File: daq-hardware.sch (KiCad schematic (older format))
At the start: 25 parts, among them J1 USB_B, J2 Micro_SD_Card_Det_Hirose_DM3AT, Q1 MMDT2222A, SW1 SW1, SW2 SW1, U1 CP2102N-A01-GQFN24, U2 ESP32-WROOM-32D

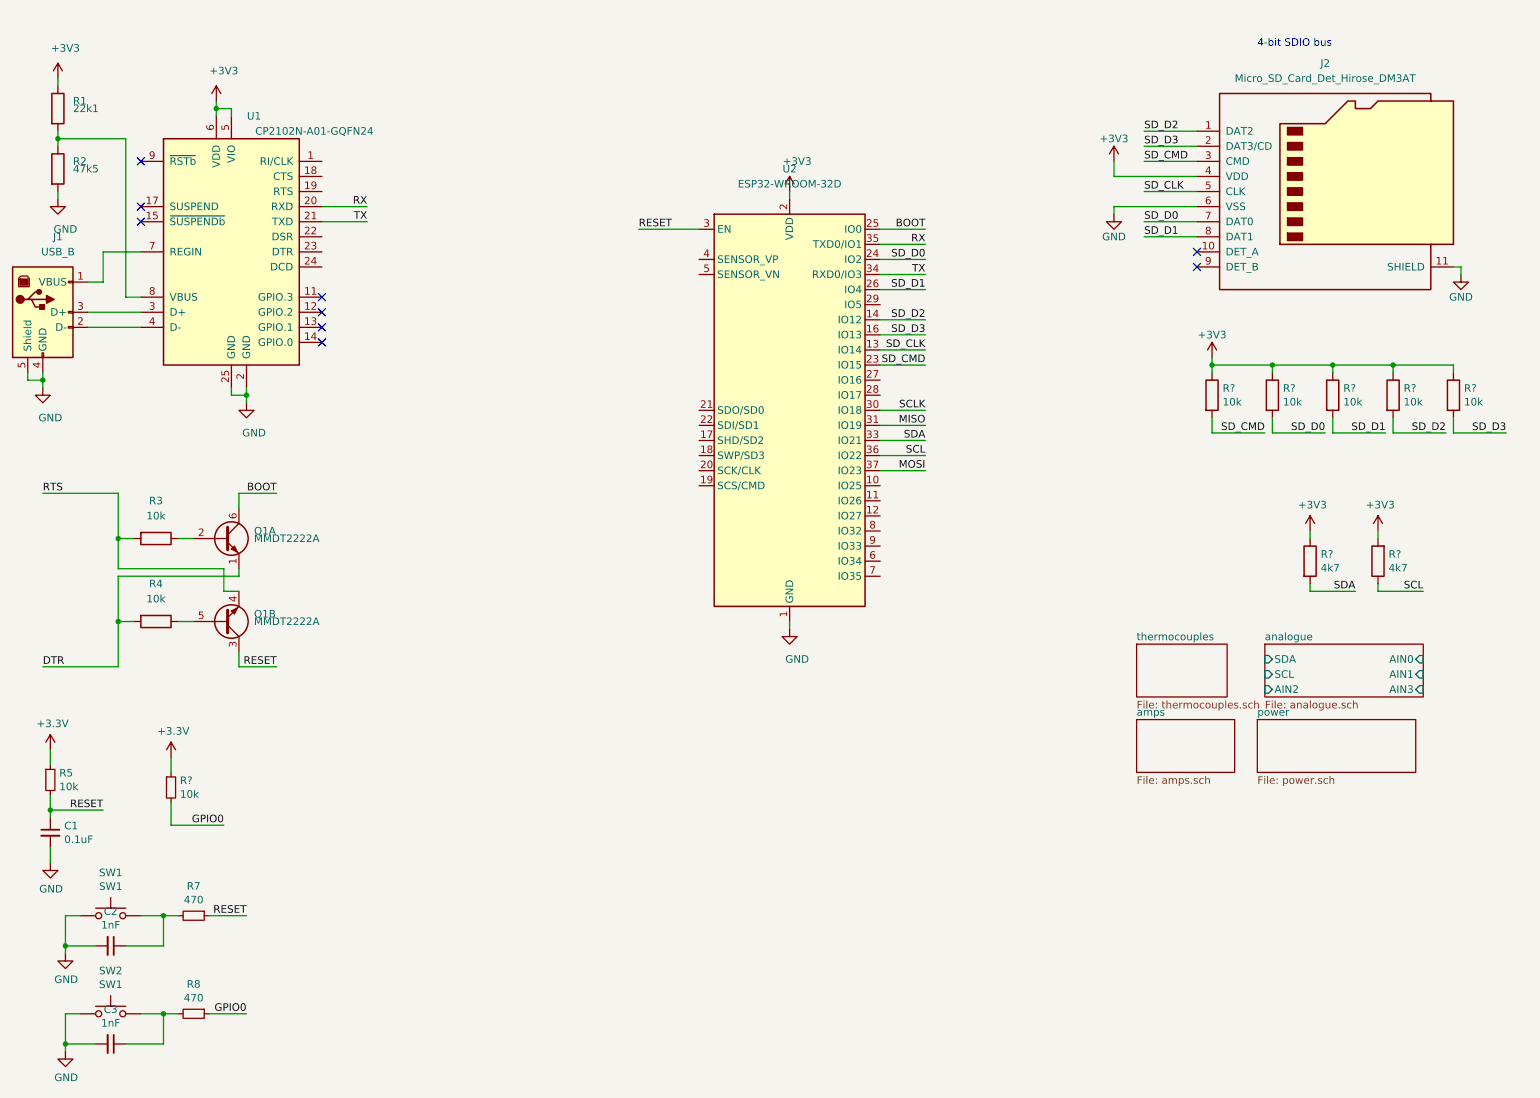
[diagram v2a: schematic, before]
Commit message: Preliminary pin mapping and amended thermocouple hierarchical sheets
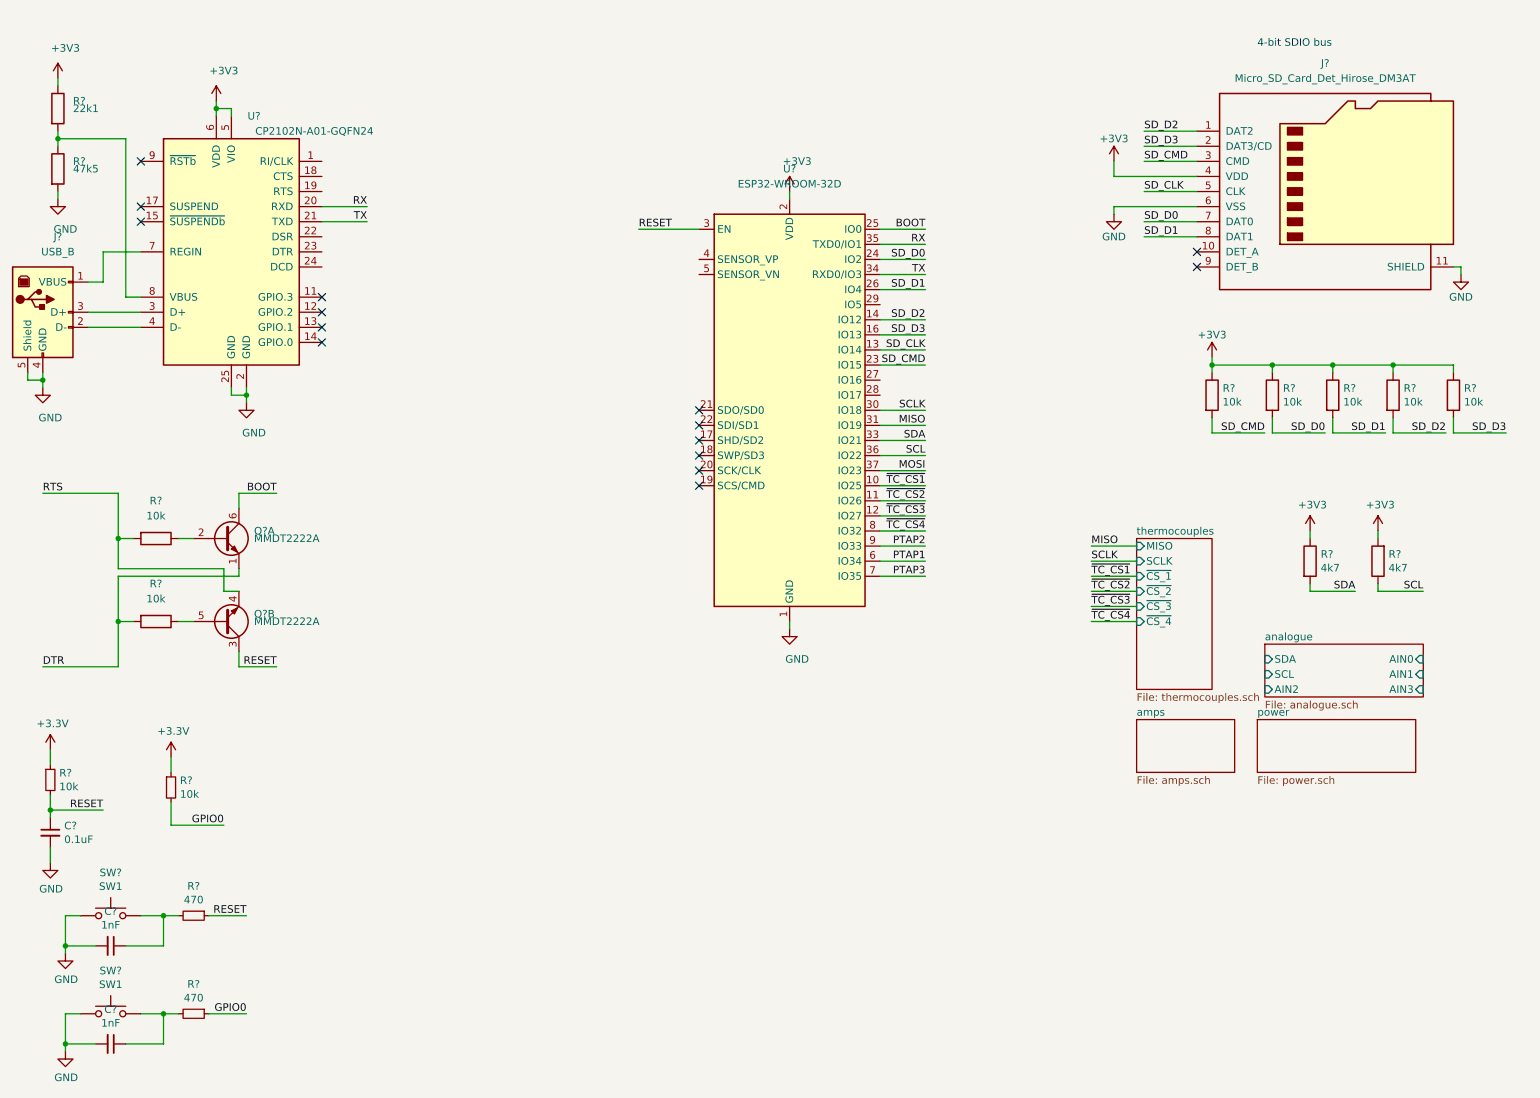
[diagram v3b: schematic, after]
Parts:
- renumbered C1 to C?, C2 to C?, C3 to C?, J1 to J?, J2 to J?, Q1 to Q?, R1 to R?, R2 to R?, R3 to R?, R4 to R?, R5 to R?, R7 to R?, R8 to R?, SW1 to SW?, SW2 to SW?, U2 to U?, U1 to U?
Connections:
- net ~TC_CS1: now reaches U?.10 (IO25)
- net ~TC_CS2: now reaches U?.11 (IO26)
- net ~TC_CS3: now reaches U?.12 (IO27)
- net PTAP1: now reaches U?.6 (IO34)
- net PTAP3: now reaches U?.7 (IO35)
- net ~TC_CS4: now reaches U?.8 (IO32)
- net PTAP2: now reaches U?.9 (IO33)
- no-connect marks 9 -> 15
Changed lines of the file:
@@
 $EndDescr
 $Comp
-L power:+3V3 #PWR0101
+L power:+3V3 #PWR?
 U 1 1 5DA618F4
 P 6300 1750
-F 0 "#PWR0101" H 6300 1600 50  0001 C CNN
+F 0 "#PWR?" H 6300 1600 50  0001 C CNN
 F 1 "+3V3" H 6350 1950 50  0000 C CNN
 F 2 "" H 6300 1750 50  0001 C CNN
@@
 	6300 1750 6300 1800
 $Comp
-L power:GND #PWR0102
+L power:GND #PWR?
 U 1 1 5DA62185
 P 6300 4650
-F 0 "#PWR0102" H 6300 4400 50  0001 C CNN
+F 0 "#PWR?" H 6300 4400 50  0001 C CNN
 F 1 "GND" H 6350 4450 50  0000 C CNN
 F 2 "" H 6300 4650 50  0001 C CNN
@@
 	6300 4650 6300 4600
 $Comp
-L Connector:USB_B J1
+L Connector:USB_B J?
 U 1 1 5DA63605
 P 1350 2550
-F 0 "J1" H 1450 3050 50  0000 C CNN
+F 0 "J?" H 1450 3050 50  0000 C CNN
 F 1 "USB_B" H 1450 2950 50  0000 C CNN
 F 2 "Connector_USB:USB_B_OST_USB-B1HSxx_Horizontal" H 1500 2500 50  0001 C CNN
@@
 $EndComp
 $Comp
-L Interface_USB:CP2102N-A01-GQFN24 U1
+L Interface_USB:CP2102N-A01-GQFN24 U?
 U 1 1 5DA64A7C
 P 2600 2150
-F 0 "U1" H 2750 3050 50  0000 C CNN
+F 0 "U?" H 2750 3050 50  0000 C CNN
 F 1 "CP2102N-A01-GQFN24" H 3150 2950 50  0000 C CNN
 F 2 "Package_DFN_QFN:QFN-24-1EP_4x4mm_P0.5mm_EP2.6x2.6mm" H 3050 1350 50  0001 L CNN
@@
 	1650 2650 2000 2650
 $Comp
-L power:GND #PWR0103
+L power:GND #PWR?
 U 1 1 5DA6844F
 P 2700 3150
-F 0 "#PWR0103" H 2700 2900 50  0001 C CNN
+F 0 "#PWR?" H 2700 2900 50  0001 C CNN
 F 1 "GND" H 2750 2950 50  0000 C CNN
 F 2 "" H 2700 3150 50  0001 C CNN
@@
 	2700 3100 2700 3050
 $Comp
-L power:GND #PWR0104
+L power:GND #PWR?
 U 1 1 5DA68DCE
 P 1350 3050
-F 0 "#PWR0104" H 1350 2800 50  0001 C CNN
+F 0 "#PWR?" H 1350 2800 50  0001 C CNN
 F 1 "GND" H 1400 2850 50  0000 C CNN
 F 2 "" H 1350 3050 50  0001 C CNN
@@
 Connection ~ 1350 3000
 $Comp
-L power:+3V3 #PWR0105
+L power:+3V3 #PWR?
 U 1 1 5DA69782
 P 2500 1150
-F 0 "#PWR0105" H 2500 1000 50  0001 C CNN
+F 0 "#PWR?" H 2500 1000 50  0001 C CNN
 F 1 "+3V3" H 2550 1350 50  0000 C CNN
 F 2 "" H 2500 1150 50  0001 C CNN
@@
 	2500 1200 2500 1250
 $Comp
-L RF_Module:ESP32-WROOM-32D U2
+L RF_Module:ESP32-WROOM-32D U?
 U 1 1 5DA60666
 P 6300 3200
-F 0 "U2" H 6300 4800 50  0000 C CNN
+F 0 "U?" H 6300 4800 50  0000 C CNN
 F 1 "ESP32-WROOM-32D" H 6300 4700 50  0000 C CNN
 F 2 "RF_Module:ESP32-WROOM-32" H 6300 1700 50  0001 C CNN
@@
 	1750 2150 2000 2150
 $Comp
-L Device:R R1
+L Device:R R?
 U 1 1 5DA6B300
 P 1450 1200
-F 0 "R1" H 1550 1250 50  0000 L CNN
+F 0 "R?" H 1550 1250 50  0000 L CNN
 F 1 "22k1" H 1550 1200 50  0000 L CNN
 F 2 "" V 1380 1200 50  0001 C CNN
@@
 $EndComp
 $Comp
-L Device:R R2
+L Device:R R?
 U 1 1 5DA6BB78
 P 1450 1600
-F 0 "R2" H 1550 1650 50  0000 L CNN
+F 0 "R?" H 1550 1650 50  0000 L CNN
 F 1 "47k5" H 1550 1600 50  0000 L CNN
 F 2 "" V 1380 1600 50  0001 C CNN
@@
 	1450 1400 1450 1450
 $Comp
-L power:GND #PWR0106
+L power:GND #PWR?
 U 1 1 5DA6CE1F
 P 1450 1800
-F 0 "#PWR0106" H 1450 1550 50  0001 C CNN
+F 0 "#PWR?" H 1450 1550 50  0001 C CNN
 F 1 "GND" H 1500 1600 50  0000 C CNN
 F 2 "" H 1450 1800 50  0001 C CNN
@@
 	1450 1800 1450 1750
 $Comp
-L power:+3V3 #PWR0107
+L power:+3V3 #PWR?
 U 1 1 5DA6D946
 P 1450 1000
-F 0 "#PWR0107" H 1450 850 50  0001 C CNN
+F 0 "#PWR?" H 1450 850 50  0001 C CNN
 F 1 "+3V3" H 1500 1200 50  0000 C CNN
 F 2 "" H 1450 1000 50  0001 C CNN
@@
 TX
 $Comp
-L Connector:Micro_SD_Card_Det_Hirose_DM3AT J2
+L Connector:Micro_SD_Card_Det_Hirose_DM3AT J?
 U 1 1 5DA72DEE
 P 9900 1750
-F 0 "J2" H 9850 2600 50  0000 C CNN
+F 0 "J?" H 9850 2600 50  0000 C CNN
 F 1 "Micro_SD_Card_Det_Hirose_DM3AT" H 9850 2500 50  0000 C CNN
 F 2 "Connector_Card:microSD_HC_Hirose_DM3AT-SF-PEJM5" H 11950 2450 50  0001 C CNN
@@
 $EndComp
 $Comp
-L power:+3V3 #PWR0108
+L power:+3V3 #PWR?
 U 1 1 5DA74F5A
 P 8450 1550
-F 0 "#PWR0108" H 8450 1400 50  0001 C CNN
+F 0 "#PWR?" H 8450 1400 50  0001 C CNN
 F 1 "+3V3" H 8450 1700 50  0000 C CNN
 F 2 "" H 8450 1550 50  0001 C CNN
@@
 	8450 1650 9000 1650
 $Comp
-L power:GND #PWR0109
+L power:GND #PWR?
 U 1 1 5DA76764
 P 8450 1900
-F 0 "#PWR0109" H 8450 1650 50  0001 C CNN
+F 0 "#PWR?" H 8450 1650 50  0001 C CNN
 F 1 "GND" H 8450 1750 50  0000 C CNN
 F 2 "" H 8450 1900 50  0001 C CNN
@@
 	8450 1850 9000 1850
 $Comp
-L Transistor_BJT:MMDT2222A Q1
+L Transistor_BJT:MMDT2222A Q?
 U 1 1 5DA77BBC
 P 2550 4050
-F 0 "Q1" H 2750 4100 50  0000 L CNN
+F 0 "Q?" H 2750 4100 50  0000 L CNN
 F 1 "MMDT2222A" H 2750 4050 50  0000 L CNN
 F 2 "Package_TO_SOT_SMD:SOT-363_SC-70-6" H 2750 4150 50  0001 C CNN
@@
 $EndComp
 $Comp
-L Transistor_BJT:MMDT2222A Q1
+L Transistor_BJT:MMDT2222A Q?
 U 2 1 5DA7899D
 P 2550 4600
-F 0 "Q1" H 2750 4550 50  0000 L CNN
+F 0 "Q?" H 2750 4550 50  0000 L CNN
 F 1 "MMDT2222A" H 2750 4600 50  0000 L CNN
 F 2 "Package_TO_SOT_SMD:SOT-363_SC-70-6" H 2750 4700 50  0001 C CNN
@@
 $EndComp
 $Comp
-L Device:R R3
+L Device:R R?
 U 1 1 5DA7B0F5
 P 2100 4050
-F 0 "R3" V 1850 4050 50  0000 C CNN
+F 0 "R?" V 1850 4050 50  0000 C CNN
 F 1 "10k" V 1950 4050 50  0000 C CNN
 F 2 "Resistor_SMD:R_0603_1608Metric" V 2030 4050 50  0001 C CNN
@@
 $EndComp
 $Comp
-L Device:R R4
+L Device:R R?
 U 1 1 5DA7B96F
 P 2100 4600
-F 0 "R4" V 1850 4600 50  0000 C CNN
+F 0 "R?" V 1850 4600 50  0000 C CNN
 F 1 "10k" V 1950 4600 50  0000 C CNN
 F 2 "Resistor_SMD:R_0603_1608Metric" V 2030 4600 50  0001 C CNN
@@
 MOSI
 $Comp
-L Device:R_Small R5
+L Device:R_Small R?
 U 1 1 5DBE20E6
 P 1400 5650
-F 0 "R5" H 1459 5696 50  0000 L CNN
+F 0 "R?" H 1459 5696 50  0000 L CNN
 F 1 "10k" H 1459 5605 50  0000 L CNN
 F 2 "" H 1400 5650 50  0001 C CNN
@@
 $EndComp
 $Comp
-L Device:C_Small C1
+L Device:C_Small C?
 U 1 1 5DBE24AB
 P 1400 6000
-F 0 "C1" H 1492 6046 50  0000 L CNN
+F 0 "C?" H 1492 6046 50  0000 L CNN
 F 1 "0.1uF" H 1492 5955 50  0000 L CNN
 F 2 "" H 1400 6000 50  0001 C CNN
@@
 	1400 5850 1400 5900
 $Comp
-L power:+3.3V #PWR0112
+L power:+3.3V #PWR?
 U 1 1 5DBE5B8C
 P 1400 5450
-F 0 "#PWR0112" H 1400 5300 50  0001 C CNN
+F 0 "#PWR?" H 1400 5300 50  0001 C CNN
 F 1 "+3.3V" H 1415 5623 50  0000 C CNN
 F 2 "" H 1400 5450 50  0001 C CNN
@@
 	1400 5450 1400 5550
 $Comp
-L power:GND #PWR0113
+L power:GND #PWR?
 U 1 1 5DBE7B6D
 P 1400 6200
-F 0 "#PWR0113" H 1400 5950 50  0001 C CNN
+F 0 "#PWR?" H 1400 5950 50  0001 C CNN
 F 1 "GND" H 1405 6027 50  0000 C CNN
 F 2 "" H 1400 6200 50  0001 C CNN
@@
 RESET
 $Comp
-L power:+3.3V #PWR0114
+L power:+3.3V #PWR?
 U 1 1 5DBEA935
 P 2200 5500
-F 0 "#PWR0114" H 2200 5350 50  0001 C CNN
+F 0 "#PWR?" H 2200 5350 50  0001 C CNN
 F 1 "+3.3V" H 2215 5673 50  0000 C CNN
 F 2 "" H 2200 5500 50  0001 C CNN
@@
 GPIO0
 $Comp
-L Switch:SW_Push SW1
+L Switch:SW_Push SW?
 U 1 1 5DBEEFD5
 P 1800 6550
-F 0 "SW1" H 1800 6835 50  0000 C CNN
+F 0 "SW?" H 1800 6835 50  0000 C CNN
 F 1 "SW1" H 1800 6744 50  0000 C CNN
 F 2 "" H 1800 6750 50  0001 C CNN
@@
 $EndComp
 $Comp
-L power:GND #PWR0115
+L power:GND #PWR?
 U 1 1 5DBF1A42
 P 1500 6800
-F 0 "#PWR0115" H 1500 6550 50  0001 C CNN
+F 0 "#PWR?" H 1500 6550 50  0001 C CNN
 F 1 "GND" H 1505 6627 50  0000 C CNN
 F 2 "" H 1500 6800 50  0001 C CNN
@@
 $EndComp
 $Comp
-L Device:C_Small C2
+L Device:C_Small C?
 U 1 1 5DBF1E6A
 P 1800 6750
-F 0 "C2" V 1571 6750 50  0000 C CNN
+F 0 "C?" V 1571 6750 50  0000 C CNN
 F 1 "1nF" V 1662 6750 50  0000 C CNN
 F 2 "" H 1800 6750 50  0001 C CNN
@@
 $EndComp
 $Comp
-L Device:R_Small R7
+L Device:R_Small R?
 U 1 1 5DBF243C
 P 2350 6550
-F 0 "R7" V 2154 6550 50  0000 C CNN
+F 0 "R?" V 2154 6550 50  0000 C CNN
 F 1 "470" V 2245 6550 50  0000 C CNN
 F 2 "" H 2350 6550 50  0001 C CNN
@@
 	2700 6550 2450 6550
 $Comp
-L Switch:SW_Push SW2
+L Switch:SW_Push SW?
 U 1 1 5DBFE9BD
 P 1800 7200
-F 0 "SW2" H 1800 7485 50  0000 C CNN
+F 0 "SW?" H 1800 7485 50  0000 C CNN
 F 1 "SW1" H 1800 7394 50  0000 C CNN
 F 2 "" H 1800 7400 50  0001 C CNN
@@
 $EndComp
 $Comp
-L power:GND #PWR0116
+L power:GND #PWR?
 U 1 1 5DBFE9C3
 P 1500 7450
-F 0 "#PWR0116" H 1500 7200 50  0001 C CNN
+F 0 "#PWR?" H 1500 7200 50  0001 C CNN
 F 1 "GND" H 1505 7277 50  0000 C CNN
 F 2 "" H 1500 7450 50  0001 C CNN
@@
 $EndComp
 $Comp
-L Device:C_Small C3
+L Device:C_Small C?
 U 1 1 5DBFE9C9
 P 1800 7400
-F 0 "C3" V 1571 7400 50  0000 C CNN
+F 0 "C?" V 1571 7400 50  0000 C CNN
 F 1 "1nF" V 1662 7400 50  0000 C CNN
 F 2 "" H 1800 7400 50  0001 C CNN
@@
 $EndComp
 $Comp
-L Device:R_Small R8
+L Device:R_Small R?
 U 1 1 5DBFE9CF
 P 2350 7200
-F 0 "R8" V 2154 7200 50  0000 C CNN
+F 0 "R?" V 2154 7200 50  0000 C CNN
 F 1 "470" V 2245 7200 50  0000 C CNN
 F 2 "" H 2350 7200 50  0001 C CNN
@@
 $EndSheet
 $Sheet
-S 8600 4750 600  350
+S 8600 4050 500  1000
 U 5DAD2AA3
 F0 "thermocouples" 50
 F1 "thermocouples.sch" 50
+F2 "~CS_1" I L 8600 4300 50
+F3 "~CS_2" I L 8600 4400 50
+F4 "~CS_3" I L 8600 4500 50
+F5 "SCLK" I L 8600 4200 50
+F6 "MISO" I L 8600 4100 50
+F7 "~CS_4" I L 8600 4600 50
 $EndSheet
 Wire Wire Line
@@
 Text Notes 9400 800  0    50   ~ 0
 4-bit SDIO bus
+Wire Wire Line
+	6900 3700 7200 3700
+Wire Wire Line
+	6900 3800 7200 3800
+Text Label 7200 3700 2    50   ~ 0
+~TC_CS1
+Text Label 7200 3800 2    50   ~ 0
+~TC_CS2
+Text Label 8300 4100 0    50   ~ 0
+MISO
+Wire Wire Line
+	8300 4100 8600 4100
+Text Label 8300 4200 0    50   ~ 0
+SCLK
+Wire Wire Line
+	8300 4200 8600 4200
+Text Label 8300 4300 0    50   ~ 0
+~TC_CS1
+Wire Wire Line
+	8300 4300 8600 4300
+Text Label 8300 4400 0    50   ~ 0
+~TC_CS2
+Wire Wire Line
+	8300 4400 8600 4400
+Wire Wire Line
+	6900 4200 7200 4200
+Wire Wire Line
+	6900 4100 7200 4100
+Text Label 7200 4200 2    50   ~ 0
+PTAP1
+Text Label 7200 4100 2    50   ~ 0
+PTAP2
+Wire Wire Line
+	6900 4300 7200 4300
+Text Label 7200 4300 2    50   ~ 0
+PTAP3
+Wire Wire Line
+	6900 3900 7200 3900
+Text Label 7200 3900 2    50   ~ 0
+~TC_CS3
+Wire Wire Line
+	6900 4000 7200 4000
+Text Label 7200 4000 2    50   ~ 0
+~TC_CS4
+Wire Wire Line
+	8600 4500 8300 4500
+Text Label 8300 4500 0    50   ~ 0
+~TC_CS3
+Wire Wire Line
+	8600 4600 8300 4600
+Text Label 8300 4600 0    50   ~ 0
+~TC_CS4
+NoConn ~ 5700 3200
+NoConn ~ 5700 3300
+NoConn ~ 5700 3400
+NoConn ~ 5700 3500
+NoConn ~ 5700 3600
+NoConn ~ 5700 3700
 $EndSCHEMATC

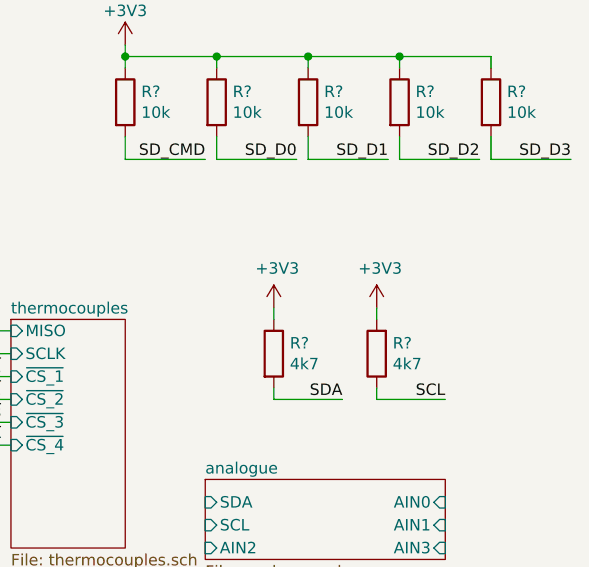
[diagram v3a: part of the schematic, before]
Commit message: Added and locked mounting holes
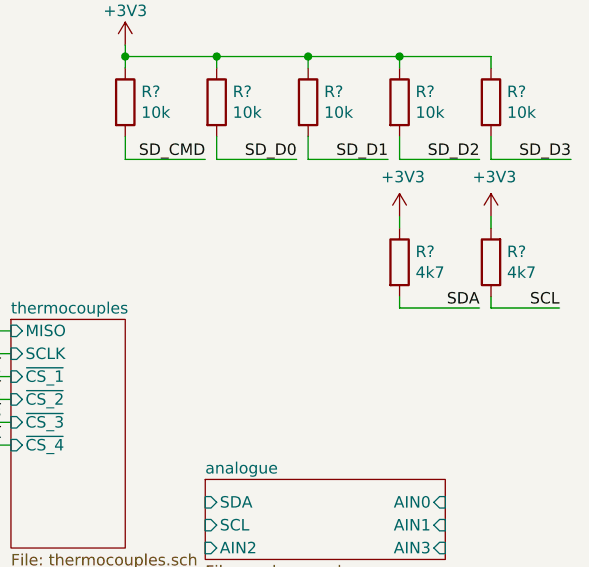
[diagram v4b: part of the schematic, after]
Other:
- moved on the sheet: R?
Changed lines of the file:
@@
 SCL
 Wire Wire Line
-	9750 4400 10050 4400
+	10300 4000 10650 4000
 Wire Wire Line
-	10200 4400 10500 4400
-Text Label 10050 4400 2    50   ~ 0
+	10700 4000 11000 4000
+Text Label 10650 4000 2    50   ~ 0
 SDA
-Text Label 10500 4400 2    50   ~ 0
+Text Label 11000 4000 2    50   ~ 0
 SCL
 $Comp
 L Device:R R?
 U 1 1 5DB5090D
-P 9750 4200
+P 10300 3800
 AR Path="/5DA926B9/5DB5090D" Ref="R?"  Part="1"
 AR Path="/5DB5090D" Ref="R?"  Part="1"
-F 0 "R?" H 9820 4246 50  0000 L CNN
-F 1 "4k7" H 9820 4155 50  0000 L CNN
-F 2 "" V 9680 4200 50  0001 C CNN
-F 3 "~" H 9750 4200 50  0001 C CNN
-	1    9750 4200
+F 0 "R?" H 10370 3846 50  0000 L CNN
+F 1 "4k7" H 10370 3755 50  0000 L CNN
+F 2 "" V 10230 3800 50  0001 C CNN
+F 3 "~" H 10300 3800 50  0001 C CNN
+	1    10300 3800
 	1    0    0    -1
 $EndComp
 Wire Wire Line
-	9750 4400 9750 4350
+	10300 4000 10300 3950
 $Comp
 L Device:R R?
 U 1 1 5DB50914
-P 10200 4200
+P 10700 3800
 AR Path="/5DA926B9/5DB50914" Ref="R?"  Part="1"
 AR Path="/5DB50914" Ref="R?"  Part="1"
-F 0 "R?" H 10130 4154 50  0000 R CNN
-F 1 "4k7" H 10130 4245 50  0000 R CNN
-F 2 "" V 10130 4200 50  0001 C CNN
-F 3 "~" H 10200 4200 50  0001 C CNN
-	1    10200 4200
+F 0 "R?" H 10630 3754 50  0000 R CNN
+F 1 "4k7" H 10630 3845 50  0000 R CNN
+F 2 "" V 10630 3800 50  0001 C CNN
+F 3 "~" H 10700 3800 50  0001 C CNN
+	1    10700 3800
 	-1   0    0    1
 $EndComp
 Wire Wire Line
-	10200 4350 10200 4400
+	10700 3950 10700 4000
 $Comp
 L power:+3V3 #PWR?
 U 1 1 5DB5091B
-P 9750 4000
+P 10300 3600
 AR Path="/5DA926B9/5DB5091B" Ref="#PWR?"  Part="1"
 AR Path="/5DB5091B" Ref="#PWR?"  Part="1"
-F 0 "#PWR?" H 9750 3850 50  0001 C CNN
-F 1 "+3V3" H 9765 4173 50  0000 C CNN
-F 2 "" H 9750 4000 50  0001 C CNN
-F 3 "" H 9750 4000 50  0001 C CNN
-	1    9750 4000
+F 0 "#PWR?" H 10300 3450 50  0001 C CNN
+F 1 "+3V3" H 10315 3773 50  0000 C CNN
+F 2 "" H 10300 3600 50  0001 C CNN
+F 3 "" H 10300 3600 50  0001 C CNN
+	1    10300 3600
 	1    0    0    -1
 $EndComp
@@
 L power:+3V3 #PWR?
 U 1 1 5DB50921
-P 10200 4000
+P 10700 3600
 AR Path="/5DA926B9/5DB50921" Ref="#PWR?"  Part="1"
 AR Path="/5DB50921" Ref="#PWR?"  Part="1"
-F 0 "#PWR?" H 10200 3850 50  0001 C CNN
-F 1 "+3V3" H 10215 4173 50  0000 C CNN
-F 2 "" H 10200 4000 50  0001 C CNN
-F 3 "" H 10200 4000 50  0001 C CNN
-	1    10200 4000
+F 0 "#PWR?" H 10700 3450 50  0001 C CNN
+F 1 "+3V3" H 10715 3773 50  0000 C CNN
+F 2 "" H 10700 3600 50  0001 C CNN
+F 3 "" H 10700 3600 50  0001 C CNN
+	1    10700 3600
 	1    0    0    -1
 $EndComp
 Wire Wire Line
-	10200 4000 10200 4050
+	10700 3600 10700 3650
 Wire Wire Line
-	9750 4000 9750 4050
+	10300 3600 10300 3650
 $Comp
 L Device:R R?
